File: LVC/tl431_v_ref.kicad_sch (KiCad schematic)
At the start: 5 parts, among them U1 TL431DBZ

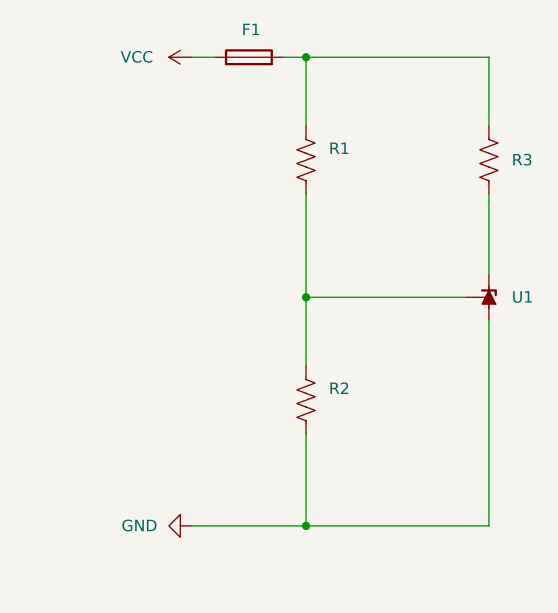
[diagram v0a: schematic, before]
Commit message: Refining Schematics
Refined the visuals of all the schematics to remove values from components. Also removed a redundant schematic.
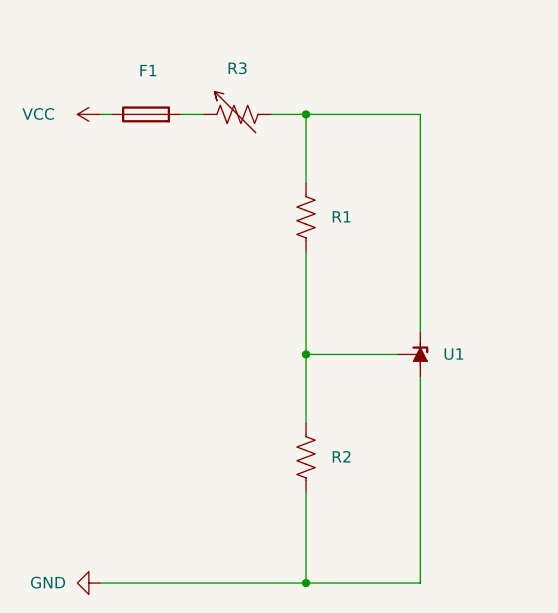
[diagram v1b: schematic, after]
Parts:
- removed R3: 6kΩ, symbol Device:R_US
- added R3: TRIMPOT, symbol Device:R_Variable_US
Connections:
- net at R1.1: now also U1.1 (K), R3.2; no longer F1.2
- net +5V renamed +4.89V
- new net: F1.2, R3.1
